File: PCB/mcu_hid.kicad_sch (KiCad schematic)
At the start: 12 parts, among them SW401 SW_MEC_5E, SW402 SW_MEC_5E, U401 AP3722AT

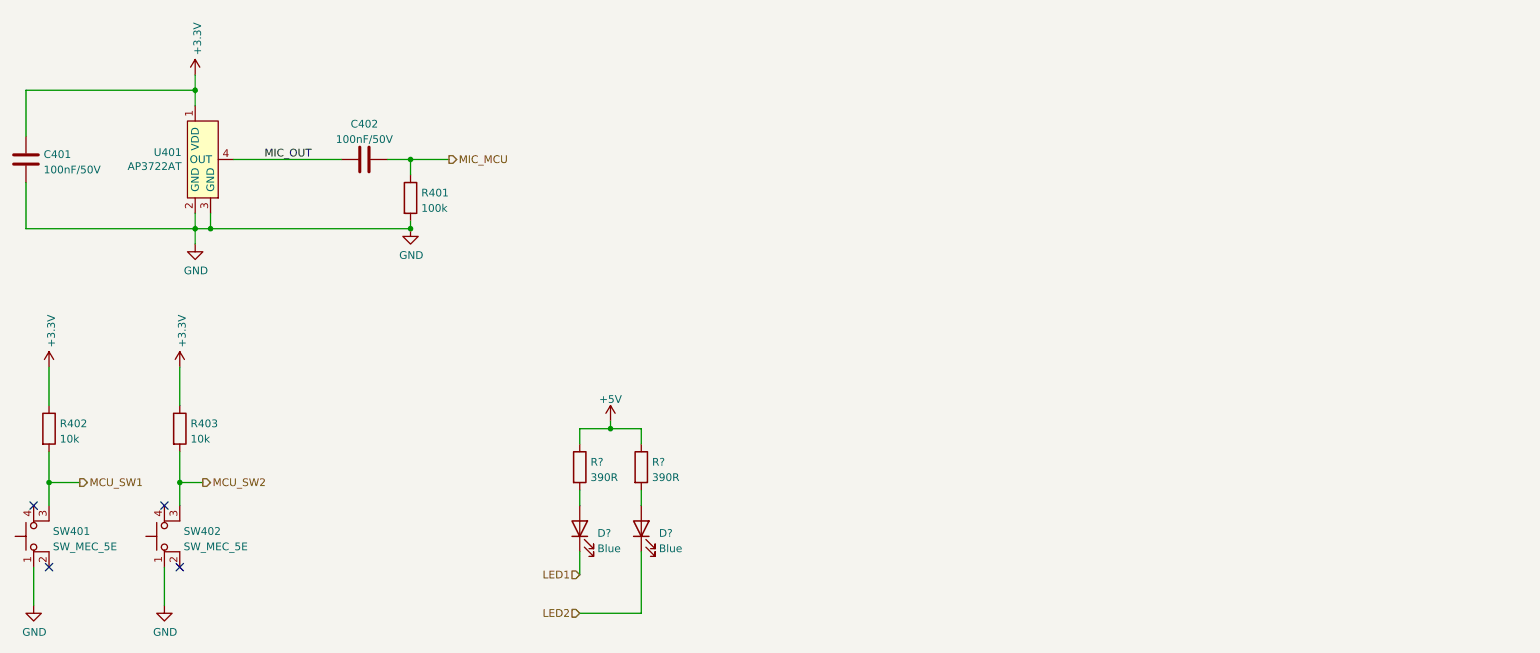
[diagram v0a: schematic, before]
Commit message: Add LEDs for each USBPD level and a microphone
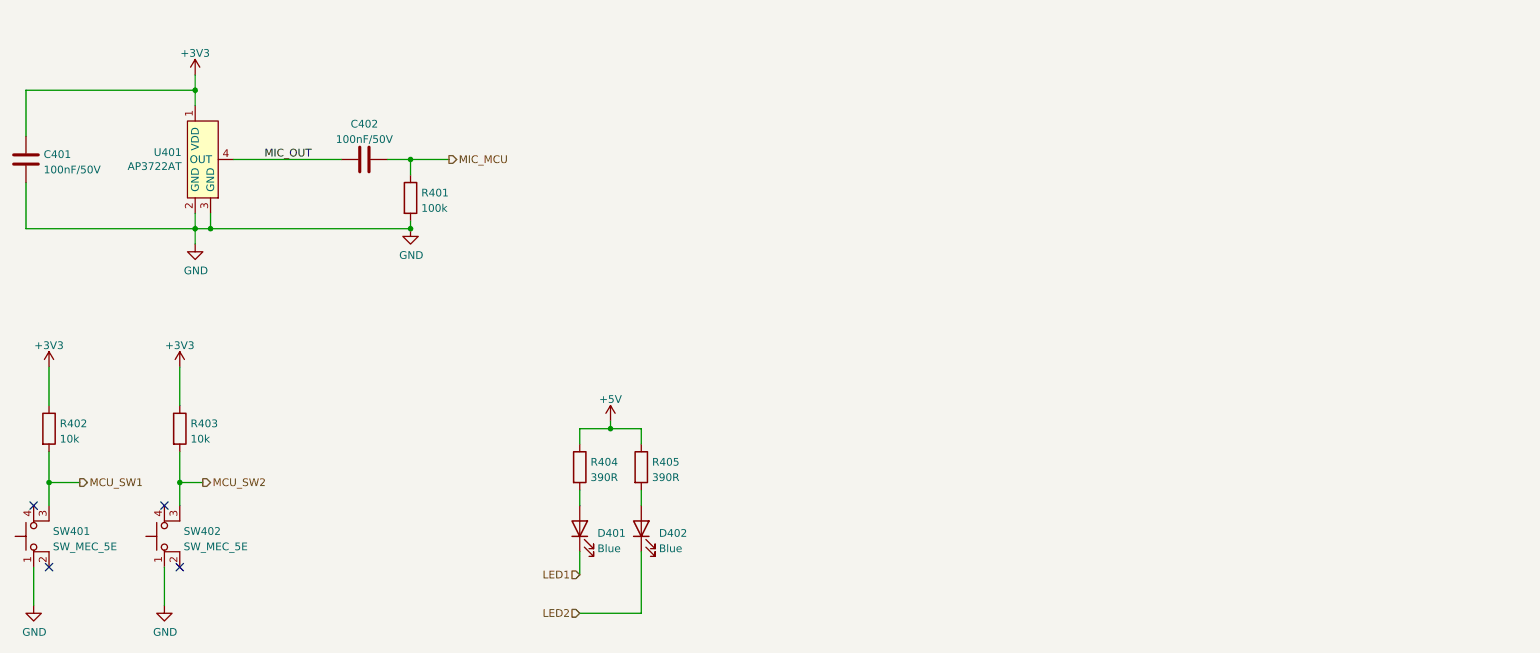
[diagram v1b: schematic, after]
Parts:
- U401: LCSC (none) -> C918198
- gave numbers to parts that had none: 4
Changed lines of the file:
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@@
     (effects (font (size 1.27 1.27)) (justify right))
+  )
+  (symbol (lib_id "power:+3V3") (at 58.42 82.55 0) (unit 1)
+    (in_bom yes) (on_board yes) (fields_autoplaced)
+    (property "Reference" "#PWR0125" (id 0) (at 58.42 86.36 0)
+      (effects (font (size 1.27 1.27)) hide)
+    )
+    (property "Value" "+3V3" (id 1) (at 58.42 78.9742 0))
+    (property "Footprint" "" (id 2) (at 58.42 82.55 0)
+      (effects (font (size 1.27 1.27)) hide)
+    )
+    (property "Datasheet" "" (id 3) (at 58.42 82.55 0)
+      (effects (font (size 1.27 1.27)) hide)
+    )
+    (pin "1")
   )
   (symbol (lib_id "power:GND") (at 60.96 62.23 0) (unit 1)
@@
     (pin "2")
   )
+  (symbol (lib_id "power:+3V3") (at 60.96 34.29 0) (unit 1)
+    (in_bom yes) (on_board yes) (fields_autoplaced)
+    (property "Reference" "#PWR?" (id 0) (at 60.96 38.1 0)
+      (effects (font (size 1.27 1.27)) hide)
+    )
+    (property "Value" "+3V3" (id 1) (at 60.96 30.7142 0))
+    (property "Footprint" "" (id 2) (at 60.96 34.29 0)
+      (effects (font (size 1.27 1.27)) hide)
+    )
+    (property "Datasheet" "" (id 3) (at 60.96 34.29 0)
+      (effects (font (size 1.27 1.27)) hide)
+    )
+    (pin "1")
+  )
   (symbol (lib_id "Device:LED") (at 134.62 109.22 90) (unit 1)
     (in_bom yes) (on_board yes) (fields_autoplaced)
-    (property "Reference" "D?" (id 0) (at 137.541 109.9728 90)
+    (property "Reference" "D402" (id 0) (at 137.541 109.9728 90)
       (effects (font (size 1.27 1.27)) (justify right))
     )
@@
   (symbol (lib_id "Device:R") (at 124.46 99.06 0) (unit 1)
     (in_bom yes) (on_board yes) (fields_autoplaced)
-    (property "Reference" "R?" (id 0) (at 126.238 98.2253 0)
+    (property "Reference" "R404" (id 0) (at 126.238 98.2253 0)
       (effects (font (size 1.27 1.27)) (justify left))
     )
@@
   (symbol (lib_id "Device:R") (at 134.62 99.06 0) (unit 1)
     (in_bom yes) (on_board yes) (fields_autoplaced)
-    (property "Reference" "R?" (id 0) (at 136.398 98.2253 0)
+    (property "Reference" "R405" (id 0) (at 136.398 98.2253 0)
       (effects (font (size 1.27 1.27)) (justify left))
     )
@@
   (symbol (lib_id "Device:LED") (at 124.46 109.22 90) (unit 1)
     (in_bom yes) (on_board yes) (fields_autoplaced)
-    (property "Reference" "D?" (id 0) (at 127.381 109.9728 90)
+    (property "Reference" "D401" (id 0) (at 127.381 109.9728 90)
       (effects (font (size 1.27 1.27)) (justify right))
     )
@@
     (pin "2")
   )
-  (symbol (lib_id "power:+3.3V") (at 36.83 82.55 0) (unit 1)
-    (in_bom yes) (on_board yes)
-    (property "Reference" "#PWR0404" (id 0) (at 36.83 86.36 0)
-      (effects (font (size 1.27 1.27)) hide)
-    )
-    (property "Value" "+3.3V" (id 1) (at 37.211 79.2988 90)
-      (effects (font (size 1.27 1.27)) (justify left))
-    )
+  (symbol (lib_id "Device:C") (at 33.02 48.26 0) (unit 1)
+    (in_bom yes) (on_board yes) (fields_autoplaced)
+    (property "Reference" "C401" (id 0) (at 35.941 47.4253 0)
+      (effects (font (size 1.27 1.27)) (justify left))
+    )
+    (property "Value" "100nF/50V" (id 1) (at 35.941 49.9622 0)
+      (effects (font (size 1.27 1.27)) (justify left))
+    )
+    (property "Footprint" "Capacitor_SMD:C_0402_1005Metric" (id 2) (at 33.9852 52.07 0)
+      (effects (font (size 1.27 1.27)) hide)
+    )
+    (property "Datasheet" "~" (id 3) (at 33.02 48.26 0)
+      (effects (font (size 1.27 1.27)) hide)
+    )
+    (property "LCSC" "C307331" (id 4) (at 33.02 48.26 0)
+      (effects (font (size 1.27 1.27)) hide)
+    )
+    (pin "1")
+    (pin "2")
+  )
+  (symbol (lib_id "power:+3V3") (at 36.83 82.55 0) (unit 1)
+    (in_bom yes) (on_board yes) (fields_autoplaced)
+    (property "Reference" "#PWR0124" (id 0) (at 36.83 86.36 0)
+      (effects (font (size 1.27 1.27)) hide)
+    )
+    (property "Value" "+3V3" (id 1) (at 36.83 78.9742 0))
     (property "Footprint" "" (id 2) (at 36.83 82.55 0)
       (effects (font (size 1.27 1.27)) hide)
@@
     (pin "1")
   )
-  (symbol (lib_id "Device:C") (at 33.02 48.26 0) (unit 1)
-    (in_bom yes) (on_board yes) (fields_autoplaced)
-    (property "Reference" "C401" (id 0) (at 35.941 47.4253 0)
-      (effects (font (size 1.27 1.27)) (justify left))
-    )
-    (property "Value" "100nF/50V" (id 1) (at 35.941 49.9622 0)
-      (effects (font (size 1.27 1.27)) (justify left))
-    )
-    (property "Footprint" "Capacitor_SMD:C_0402_1005Metric" (id 2) (at 33.9852 52.07 0)
-      (effects (font (size 1.27 1.27)) hide)
-    )
-    (property "Datasheet" "~" (id 3) (at 33.02 48.26 0)
-      (effects (font (size 1.27 1.27)) hide)
-    )
-    (property "LCSC" "C307331" (id 4) (at 33.02 48.26 0)
-      (effects (font (size 1.27 1.27)) hide)
-    )
-    (pin "1")
-    (pin "2")
-  )
   (symbol (lib_id "power:GND") (at 55.88 121.92 0) (unit 1)
     (in_bom yes) (on_board yes)
-    (property "Reference" "#PWR0407" (id 0) (at 55.88 128.27 0)
+    (property "Reference" "#PWR0408" (id 0) (at 55.88 128.27 0)
       (effects (font (size 1.27 1.27)) hide)
     )
@@
   (symbol (lib_id "power:GND") (at 34.29 121.92 0) (unit 1)
     (in_bom yes) (on_board yes)
-    (property "Reference" "#PWR0406" (id 0) (at 34.29 128.27 0)
+    (property "Reference" "#PWR0407" (id 0) (at 34.29 128.27 0)
       (effects (font (size 1.27 1.27)) hide)
     )
@@
     (pin "1")
   )
-  (symbol (lib_id "power:+3.3V") (at 58.42 82.55 0) (unit 1)
-    (in_bom yes) (on_board yes)
-    (property "Reference" "#PWR0405" (id 0) (at 58.42 86.36 0)
-      (effects (font (size 1.27 1.27)) hide)
-    )
-    (property "Value" "+3.3V" (id 1) (at 58.801 79.2988 90)
-      (effects (font (size 1.27 1.27)) (justify left))
-    )
-    (property "Footprint" "" (id 2) (at 58.42 82.55 0)
-      (effects (font (size 1.27 1.27)) hide)
-    )
-    (property "Datasheet" "" (id 3) (at 58.42 82.55 0)
-      (effects (font (size 1.27 1.27)) hide)
-    )
-    (pin "1")
-  )
-  (symbol (lib_id "power:+3.3V") (at 60.96 34.29 0) (unit 1)
-    (in_bom yes) (on_board yes)
-    (property "Reference" "#PWR0401" (id 0) (at 60.96 38.1 0)
-      (effects (font (size 1.27 1.27)) hide)
-    )
-    (property "Value" "+3.3V" (id 1) (at 61.341 31.0388 90)
-      (effects (font (size 1.27 1.27)) (justify left))
-    )
-    (property "Footprint" "" (id 2) (at 60.96 34.29 0)
-      (effects (font (size 1.27 1.27)) hide)
-    )
-    (property "Datasheet" "" (id 3) (at 60.96 34.29 0)
-      (effects (font (size 1.27 1.27)) hide)
-    )
-    (pin "1")
-  )
   (symbol (lib_id "Device:R") (at 58.42 92.71 0) (unit 1)
     (in_bom yes) (on_board yes) (fields_autoplaced)
@@
   (symbol (lib_id "power:+5V") (at 129.54 91.44 0) (unit 1)
     (in_bom yes) (on_board yes) (fields_autoplaced)
-    (property "Reference" "#PWR?" (id 0) (at 129.54 95.25 0)
+    (property "Reference" "#PWR0406" (id 0) (at 129.54 95.25 0)
       (effects (font (size 1.27 1.27)) hide)
     )
@@
       (effects (font (size 1.27 1.27)) hide)
     )
+    (property "LCSC" "C918198" (id 4) (at 62.23 44.45 0)
+      (effects (font (size 1.27 1.27)) hide)
+    )

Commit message: Fix review comments
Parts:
- added C403, C404: 100nF/50V, Capacitor_SMD:C_0402_1005Metric, symbol Device:C
- added M101: Fan_4pin, Connector_PinHeader_2.54mm:PinHeader_1x04_P2.54mm_Vertical_SMD_Pin1Left, symbol Motor:Fan_4pin
- U401: footprint Skrooter_footprints:AP3722AT -> SkrooterFootprints:AP3722AT
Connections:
- net +5V: now also M101.2 (+)
- net GND: now also C403.2, C404.2, M101.1 (-)
- net MCU_SW1: now also C403.1
- net MCU_SW2: now also C404.1
- new net Fan_PWM: M101.4 (PWM)
- new net Fan_Tachometer: M101.3 (Tacho)
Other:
- moved on the sheet: R403, SW402

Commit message: Final fixes before production
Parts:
- U401: symbol stm32ledbreakout-rescue:AP3722AT-Skrooter -> Skrooterlib:AP3722AT
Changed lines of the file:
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@@
     )
   )
-  (symbol (lib_id "stm32ledbreakout-rescue:AP3722AT-Skrooter") (at 62.23 44.45 0) (unit 1)
+  (symbol (lib_id "Skrooterlib:AP3722AT") (at 62.23 44.45 0) (unit 1)
     (in_bom yes) (on_board yes) (dnp no)
     (property "Reference" "U401" (at 58.7248 47.0916 0)
